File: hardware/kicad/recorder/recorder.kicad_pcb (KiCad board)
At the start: 4 copper layers, 64 x 86 mm, 60 parts, among them J1 UART0, J2 USB_C_16P, J3 microSD, SW1 record, U1 ESP32-S3-MINI-1U-N8, U2 ES8311, U3 MCP73831-2-OT, U4 AP2112K-3.3, U5 AP22804AW5, U6 NS4150B, U7 USBLC6-2SC6, U8 LP5907MFX-3.3, Y1 12.288MHz

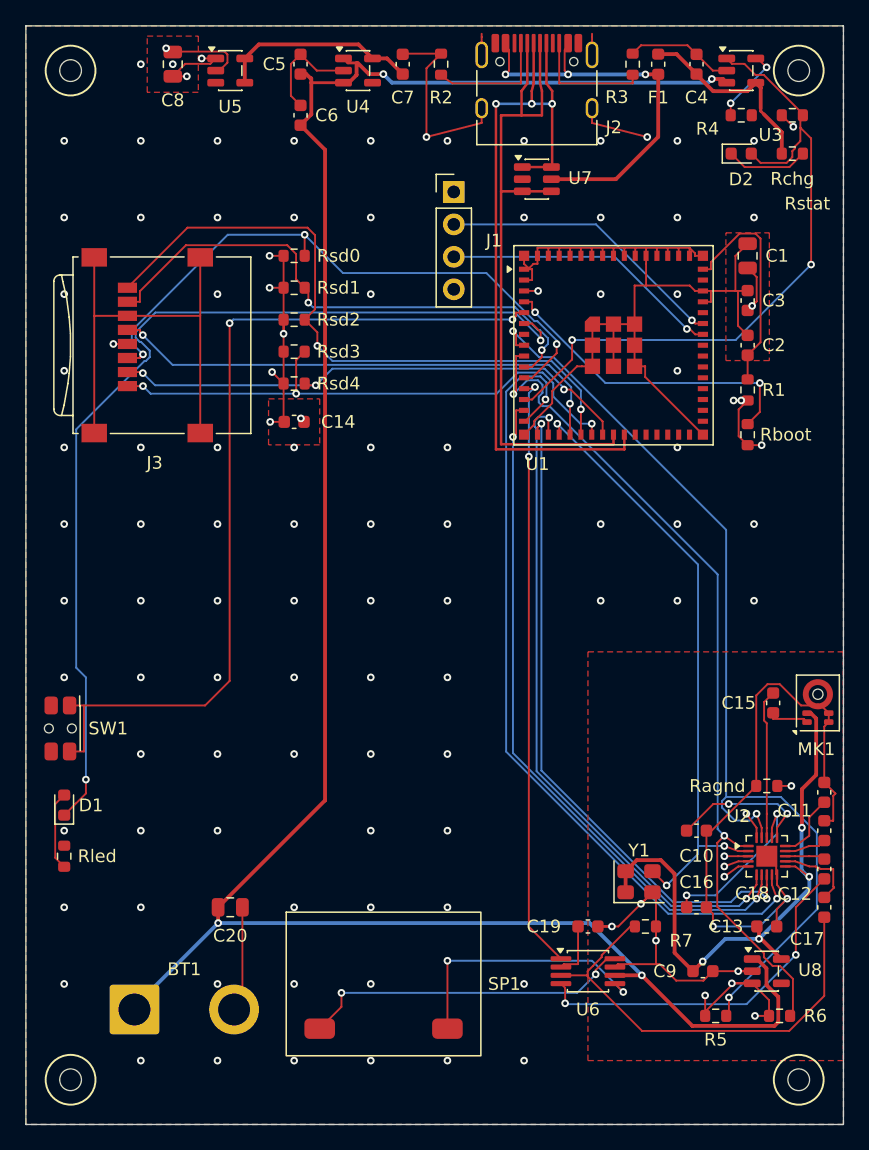
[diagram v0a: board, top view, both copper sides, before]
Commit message: Pick a JLCPCB-placeable KELIKING speaker for SP1
The 15x11 placeholder could not go on the SMT line. The KLJ-01304T land, shifted pouch, and lid grille let JLC place C18186315 on a DRC-clean board.
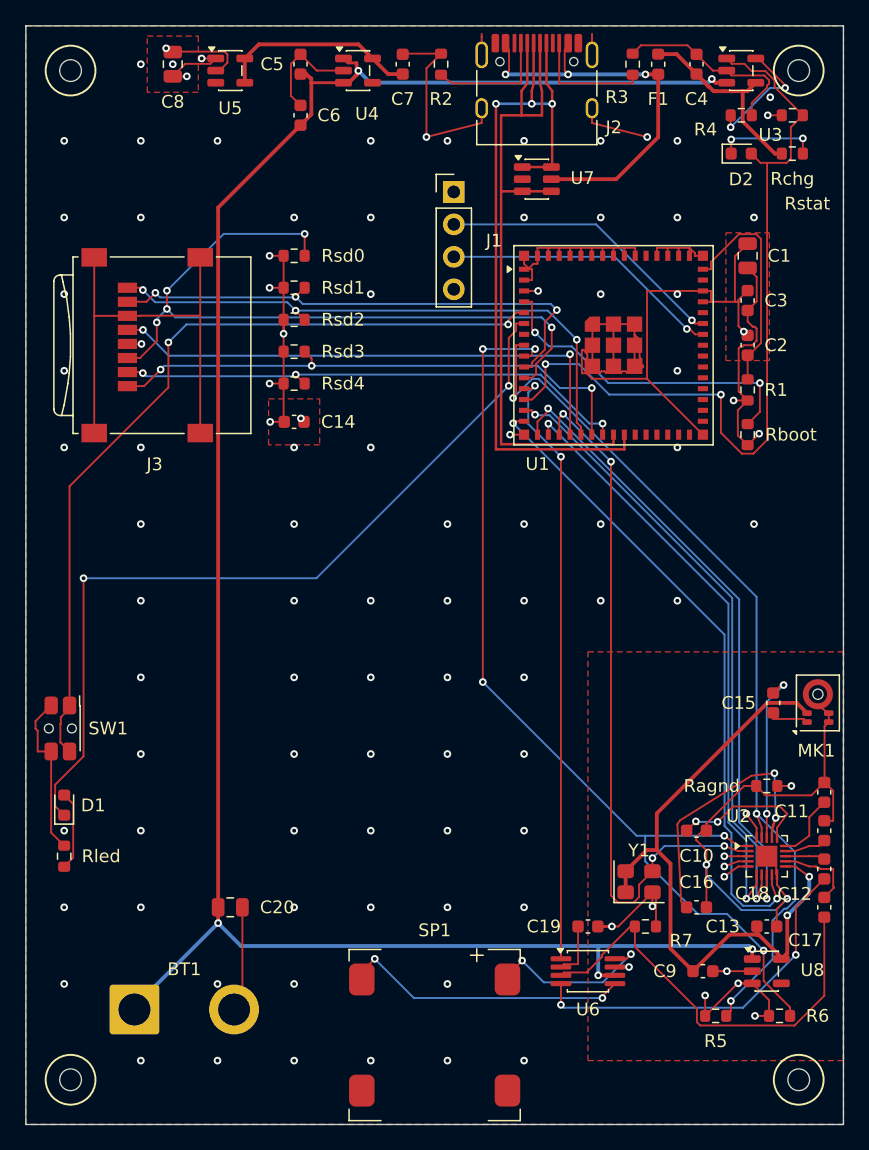
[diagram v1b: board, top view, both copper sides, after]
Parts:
- SP1: value 1511 -> KLJ-01304T-08R07W; footprint PSV:Speaker_15x11mm -> PSV:Speaker_KLJ-01304T
- moved SP1 5.66 mm to (0.00, 36.0)
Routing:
- net GND: track 203.2 -> 217.9 mm, vias 94 -> 86
- net I2S_DOUT: track 64.7 -> 51.0 mm
- net /Audio/SPK_P: track 26.2 -> 13.5 mm
- net LED: track 77.4 -> 65.0 mm
- net VBAT: track 172.4 -> 162.2 mm, vias 4 -> 5
- net I2C_SCL: track 67.7 -> 77.6 mm, vias 2 -> 5
- net CHG_STAT: track 54.0 -> 63.4 mm
- net /Audio/MIC_N: track 13.5 -> 21.6 mm
- net SD_CMD: track 49.4 -> 57.4 mm, vias 3 -> 5
- net VDD33: track 56.8 -> 64.8 mm, vias 21 -> 19
- net I2C_SDA: track 77.6 -> 69.9 mm
- net I2S_MCLK: track 48.2 -> 55.1 mm, vias 3 -> 4
- net I2S_BCLK: track 53.3 -> 46.6 mm
- net SD_D1: track 51.8 -> 45.4 mm, vias 2 -> 3
- net 3V3A: track 46.8 -> 53.1 mm, vias 4 -> 2
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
